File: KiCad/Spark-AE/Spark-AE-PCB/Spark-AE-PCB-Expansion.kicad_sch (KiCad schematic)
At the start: 15 parts, among them J6 USB_C_Receptacle_USB2.0_14P, J7 I2C_IN, J8 I2C_OUT, J9 Conn_02x06_Top_Bottom

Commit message: assigned footprints & sorted ratsnest
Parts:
- removed J6: USB_C_Receptacle_USB2.0_14P, symbol Connector:USB_C_Receptacle_USB2.0_14P
- added USB1: USB_C_Receptacle_G-Switch_GT-USB-7038A, clectric-diy:USB_C_Receptacle_G-Switch_GT-USB-7038A, symbol clectric-diy:USB_C_Receptacle_G-Switch_GT-USB-7038A
- C19: renamed from C14; footprint (none) -> Capacitor_SMD:C_0603_1608Metric
- C20: renamed from C13; footprint (none) -> Capacitor_SMD:C_0805_2012Metric
- C21: renamed from C15; footprint (none) -> Capacitor_SMD:C_0603_1608Metric
- C22: renamed from C16; footprint (none) -> Capacitor_SMD:C_0805_2012Metric
- C23: renamed from C17; footprint (none) -> Capacitor_SMD:C_0603_1608Metric
- C24: renamed from C18; footprint (none) -> Capacitor_SMD:C_0805_2012Metric
- C25: renamed from C19; footprint (none) -> Capacitor_SMD:C_0603_1608Metric
- C26: renamed from C20; footprint (none) -> Capacitor_SMD:C_0805_2012Metric
- D3: renamed from D2; value 1N5817 -> 2214; footprint Diode_THT:D_DO-41_SOD81_P10.16mm_Horizontal -> Diode_SMD:D_SMA
- J6: renamed from J7; footprint (none) -> Connector_JST:JST_SH_SM04B-SRSS-TB_1x04-1MP_P1.00mm_Horizontal
- J7: renamed from J8; footprint (none) -> Connector_JST:JST_SH_SM04B-SRSS-TB_1x04-1MP_P1.00mm_Horizontal
- J8: renamed from J9; footprint (none) -> Connector_PinHeader_2.54mm:PinHeader_2x06_P2.54mm_Vertical
- R45: renamed from R38; footprint (none) -> Resistor_SMD:R_0603_1608Metric
- R46: renamed from R39; footprint (none) -> Resistor_SMD:R_0603_1608Metric
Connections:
- net +5V: now also USB1.A4B9 (VBUS), USB1.A9B4 (VBUS)
- net GNDD: now also R45.1, USB1.17 (SH), USB1.18 (SH), USB1.19 (SH), USB1.20 (SH), USB1.A12B1 (GND), USB1.A1B12 (GND); no longer R45.2
- net USB_D+: now also USB1.A6 (D+), USB1.B6 (D+)
- net USB_D-: now also USB1.A7 (D-), USB1.B7 (D-)
- net at R46.1: now also USB1.B5 (CC2)
- new net: R45.2, USB1.A5 (CC1)
- no-connect marks 6 -> 8
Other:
- moved on the sheet: C19, C20, C21, C22, C23, C24, C25, C26, D3, J6, J7, J8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

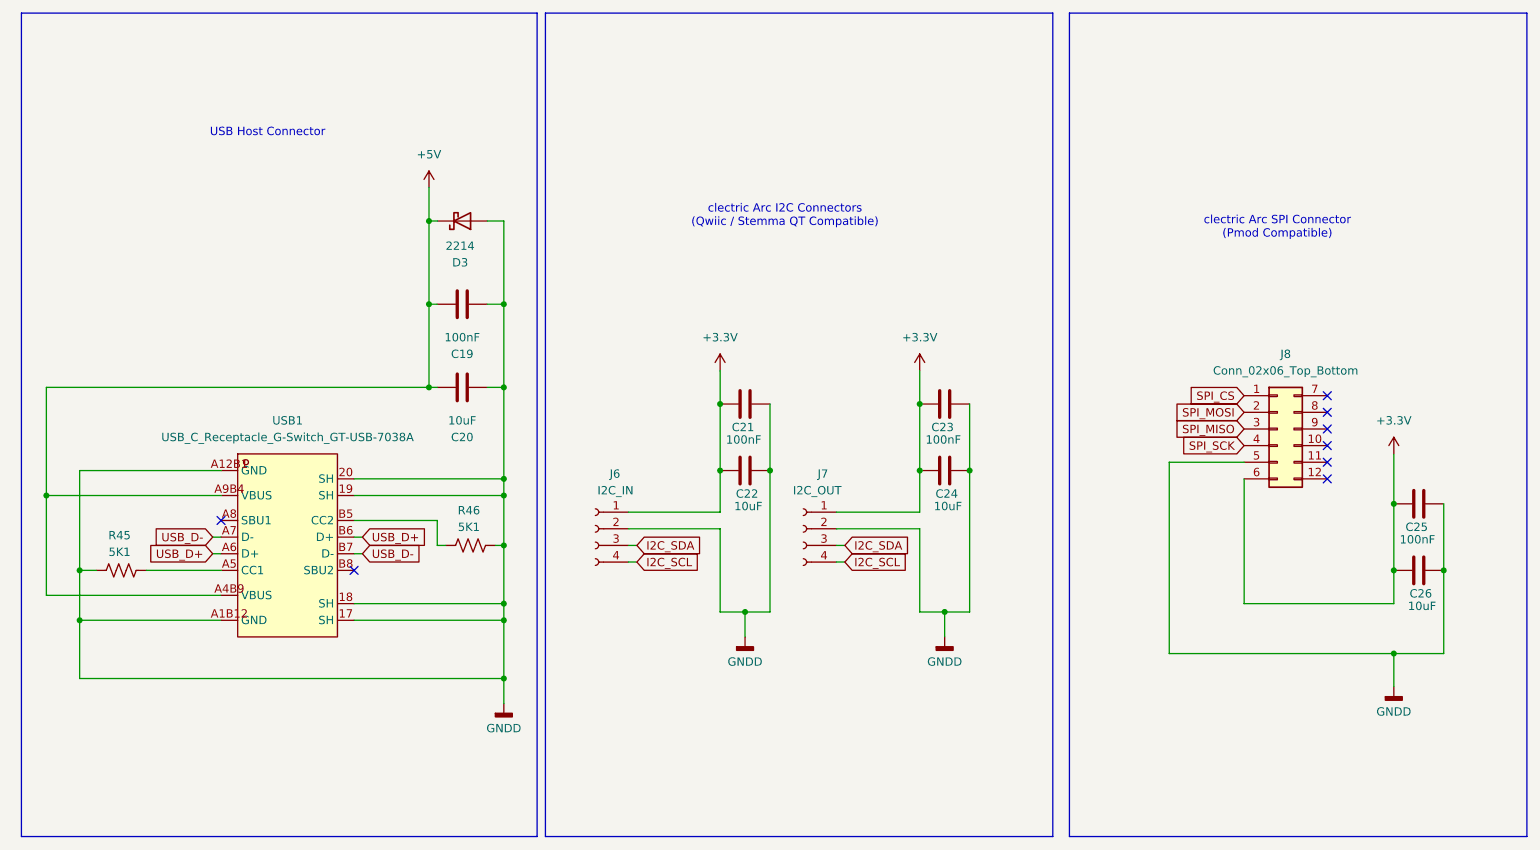
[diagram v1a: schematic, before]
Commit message: schematic 100% complete. pcb layout around 50% complete.
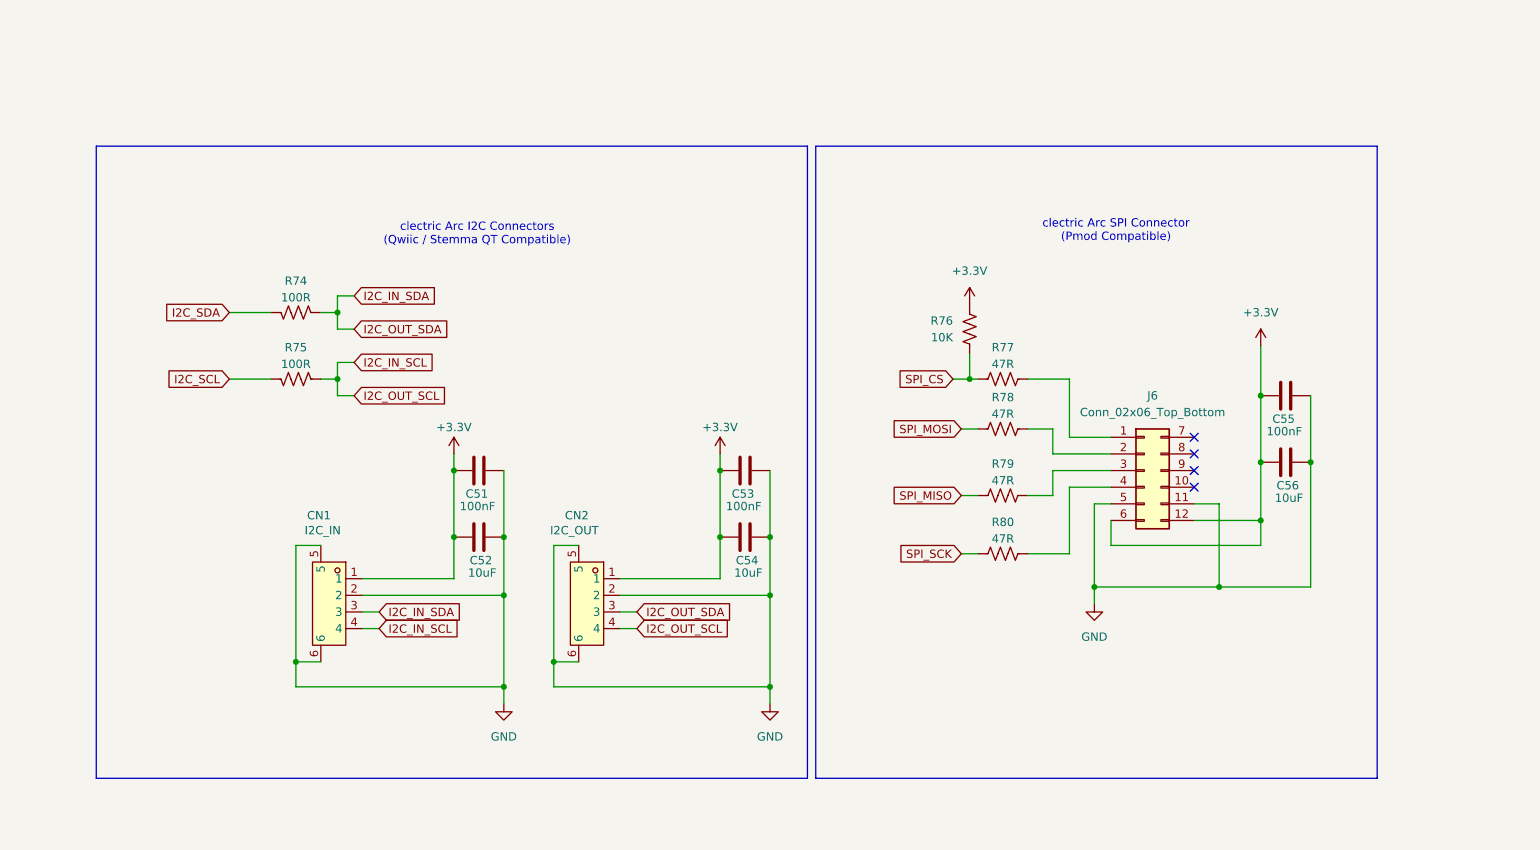
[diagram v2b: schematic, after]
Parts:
- removed C19: 100nF, Capacitor_SMD:C_0603_1608Metric, symbol Device:C
- removed C20: 10uF, Capacitor_SMD:C_0805_2012Metric, symbol Device:C
- removed D3: 2214, Diode_SMD:D_SMA, symbol Diode:1N5817
- removed J6: I2C_IN, Connector_JST:JST_SH_SM04B-SRSS-TB_1x04-1MP_P1.00mm_Horizontal, symbol Connector:Conn_01x04_Socket
- removed J7: I2C_OUT, Connector_JST:JST_SH_SM04B-SRSS-TB_1x04-1MP_P1.00mm_Horizontal, symbol Connector:Conn_01x04_Socket
- removed R45, R46: 5K1, Resistor_SMD:R_0603_1608Metric, symbol Device:R_US
- removed USB1: USB_C_Receptacle_G-Switch_GT-USB-7038A, clectric-diy:USB_C_Receptacle_G-Switch_GT-USB-7038A, symbol clectric-diy:USB_C_Receptacle_G-Switch_GT-USB-7038A
- added CN1: I2C_IN, clectric-diy:Connector_JST_BM04B-SRSS-TBT-LF-SN, symbol clectric-diy:Connector_JST_BM04B-SRSS-TBT(LF)(SN)
- added CN2: I2C_OUT, clectric-diy:Connector_JST_BM04B-SRSS-TBT-LF-SN, symbol clectric-diy:Connector_JST_BM04B-SRSS-TBT(LF)(SN)
- added R74, R75: 100R, Resistor_SMD:R_0603_1608Metric, symbol Device:R_US
- added R76: 10K, Resistor_SMD:R_0603_1608Metric, symbol Device:R_US
- added R77, R78, R79, R80: 47R, Resistor_SMD:R_0603_1608Metric, symbol Device:R_US
- C52: renamed from C22; footprint Capacitor_SMD:C_0805_2012Metric -> Capacitor_SMD:C_0603_1608Metric
- C54: renamed from C24; footprint Capacitor_SMD:C_0805_2012Metric -> Capacitor_SMD:C_0603_1608Metric
- C56: renamed from C26; footprint Capacitor_SMD:C_0805_2012Metric -> Capacitor_SMD:C_0603_1608Metric
- renumbered C21 to C51, C23 to C53, C25 to C55, J8 to J6
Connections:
- net GNDD is gone; now on net GND: C51.2, C52.2, C53.2, C54.2, C55.2, C56.2, J6.5 (Pin_5)
- net +3.3V: now also J6.12 (Pin_12), CN1.1, CN2.1, R76.1
- net I2C_SCL: now also R75.2
- net I2C_SDA: now also R74.2
- net SPI_CS: now also R76.2, R77.1; no longer J6.1 (Pin_1)
- net SPI_MISO: now also R79.1; no longer J6.3 (Pin_3)
- net SPI_MOSI: now also R78.1; no longer J6.2 (Pin_2)
- net SPI_SCK: now also R80.1; no longer J6.4 (Pin_4)
- net GND: now reaches J6.11 (Pin_11)
- net GND: now also CN1.2, CN1.5, CN1.6, CN2.2, CN2.5, CN2.6
- new net: J6.4 (Pin_4), R80.2
- new net: J6.1 (Pin_1), R77.2
- new net: J6.2 (Pin_2), R78.2
- new net: J6.3 (Pin_3), R79.2
- new net I2C_IN_SCL: CN1.4, CN2.4, R75.1
- new net I2C_IN_SDA: CN1.3, CN2.3, R74.1
- no-connect marks 8 -> 4
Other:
- note removed: "USB Host Connector"
- moved on the sheet: C51, C52, C53, C54, C55, C56, J6

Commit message: continuing to plug away at pcb layout
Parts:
- renumbered C51 to C49, C52 to C50, C53 to C51, C54 to C52, C55 to C53, C56 to C54
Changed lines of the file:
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@@
 		(on_board yes)
 		(dnp no)
-		(property "Reference" "C52"
+		(property "Reference" "C50"
 			(at 109.982 115.316 90)
 			(effects
@@
 			(project "Spark-AE-PCB"
 				(path "/b249adcd-2848-4e56-9615-c4f1b6083abe/068f8c39-4a2c-47d3-9aa1-f68922ad9282"
-					(reference "C52")
+					(reference "C50")
 					(unit 1)
 				)
@@
 		(on_board yes)
 		(dnp no)
-		(property "Reference" "C56"
+		(property "Reference" "C54"
 			(at 233.172 103.886 90)
 			(effects
@@
 			(project "Spark-AE-PCB"
 				(path "/b249adcd-2848-4e56-9615-c4f1b6083abe/068f8c39-4a2c-47d3-9aa1-f68922ad9282"
-					(reference "C56")
+					(reference "C54")
 					(unit 1)
 				)
@@
 		(on_board yes)
 		(dnp no)
-		(property "Reference" "C54"
+		(property "Reference" "C52"
 			(at 150.622 115.316 90)
 			(effects
@@
 			(project "Spark-AE-PCB"
 				(path "/b249adcd-2848-4e56-9615-c4f1b6083abe/068f8c39-4a2c-47d3-9aa1-f68922ad9282"
-					(reference "C54")
+					(reference "C52")
 					(unit 1)
 				)
@@
 		(on_board yes)
 		(dnp no)
-		(property "Reference" "C53"
+		(property "Reference" "C51"
 			(at 146.558 105.156 90)
 			(effects
@@
 			(project ""
 				(path "/b249adcd-2848-4e56-9615-c4f1b6083abe/068f8c39-4a2c-47d3-9aa1-f68922ad9282"
-					(reference "C53")
+					(reference "C51")
 					(unit 1)
 				)
@@
 		(on_board yes)
 		(dnp no)
-		(property "Reference" "C51"
+		(property "Reference" "C49"
 			(at 105.918 105.156 90)
 			(effects
@@
 			(project "Spark-AE-PCB"
 				(path "/b249adcd-2848-4e56-9615-c4f1b6083abe/068f8c39-4a2c-47d3-9aa1-f68922ad9282"
-					(reference "C51")
+					(reference "C49")
 					(unit 1)
 				)
@@
 		(on_board yes)
 		(dnp no)
-		(property "Reference" "C55"
+		(property "Reference" "C53"
 			(at 229.108 93.726 90)
 			(effects
@@
 			(project "Spark-AE-PCB"
 				(path "/b249adcd-2848-4e56-9615-c4f1b6083abe/068f8c39-4a2c-47d3-9aa1-f68922ad9282"
-					(reference "C55")
-					(unit 1)
-				)
+					(reference "C53")
+					(unit 1)
+				)

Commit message: pcb layout complete. ready for final pre-fab confirmation.
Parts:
- removed C49: 100nF, Capacitor_SMD:C_0603_1608Metric, symbol Device:C
- removed C50: 10uF, Capacitor_SMD:C_0603_1608Metric, symbol Device:C
- J6: value Conn_02x06_Top_Bottom -> SPI
- renumbered C51 to C49, C52 to C50, C53 to C51, C54 to C52, R74 to R76, R75 to R77, R76 to R78, R77 to R79, R78 to R80, R79 to R81, R80 to R82
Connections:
- net +3.3V: now also C49.2, C50.2, CN1.2, CN2.2; no longer C49.1, C50.1, CN1.1, CN2.1
- net GND: now also C49.1, C50.1, CN1.1, CN2.1; no longer C49.2, C50.2, CN1.2, CN2.2
- net I2C_IN_SCL renamed I2C_SCL_BUS
- net I2C_IN_SDA renamed I2C_SDA_BUS
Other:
- moved on the sheet: C49, C50, CN1, CN2, R76, R77
